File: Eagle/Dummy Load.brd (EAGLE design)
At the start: 100 x 50 mm, 60 parts, among them IC1 LM324D, IC2 AMS1117, IC3 LM35CZ, J2 DCJ0202, X1 MINI-USB-32005-301

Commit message: Update Proteus Files & Latest BRD Version
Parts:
- moved GOLD_ORB_SM2 2.00 mm to (50.1, 24.4)
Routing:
- net VCC: track 280.7 -> 344.2 mm
- net VG: track 76.8 -> 81.7 mm
- net N$15: track 16.8 -> 17.7 mm
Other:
- board text added: "FAN"

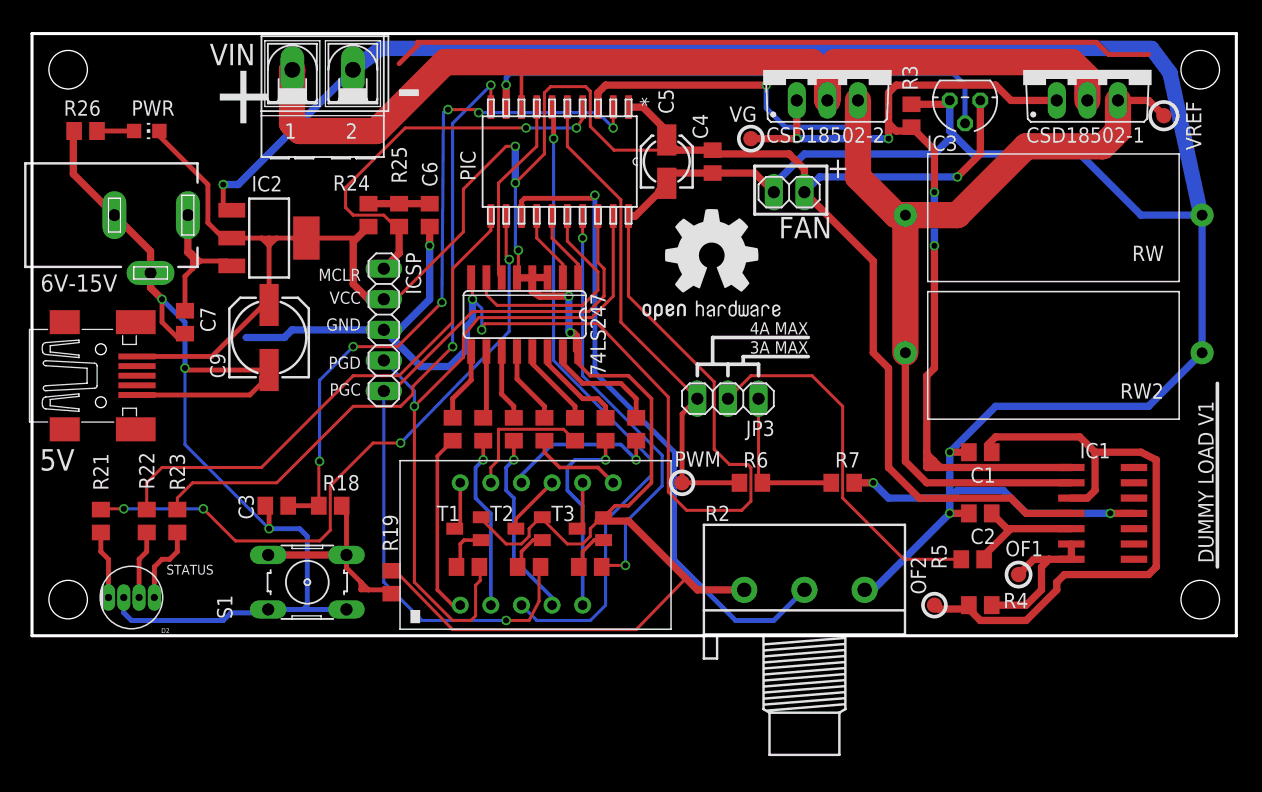
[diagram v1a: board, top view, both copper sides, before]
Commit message: Update all files to V1.1
Implement Gate Series Resistor on MOSFET, to prevent the oscillators in
the output. Also implement new OPAMP LMC662, and new desing of PCB
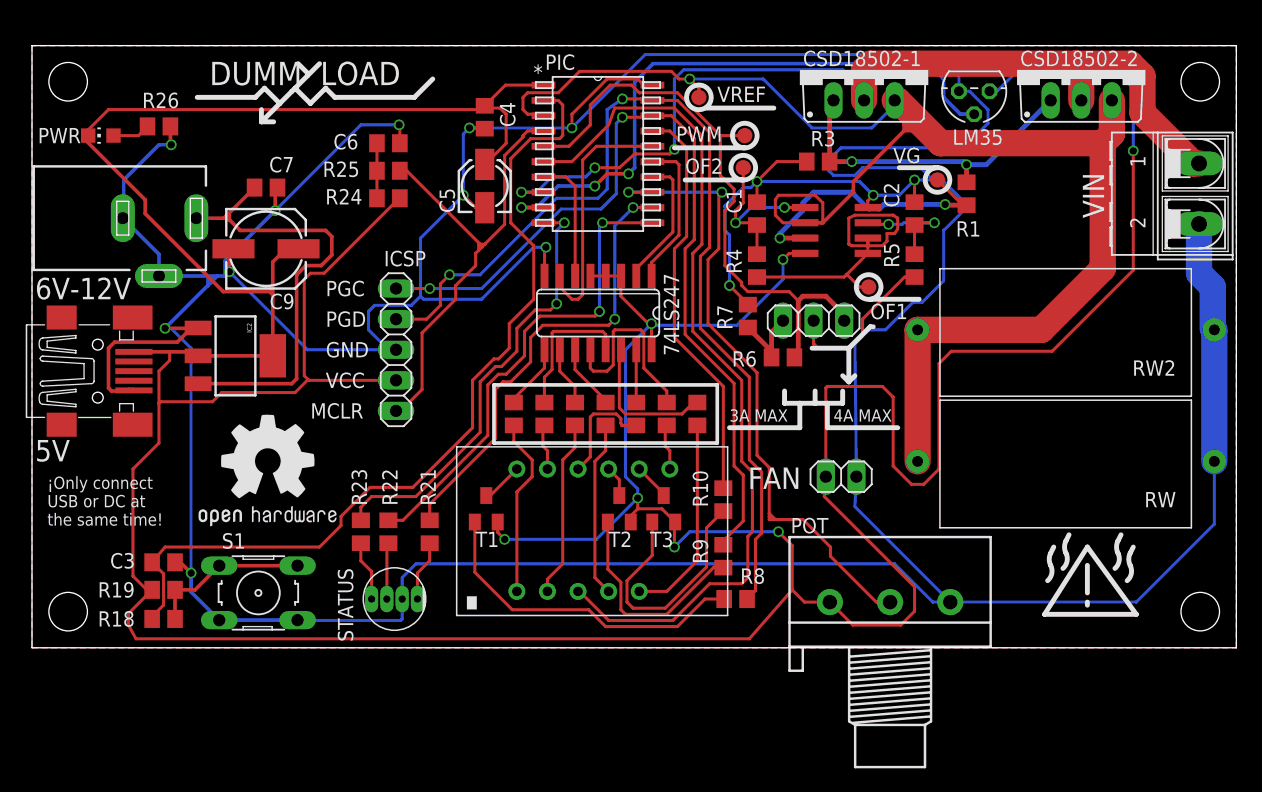
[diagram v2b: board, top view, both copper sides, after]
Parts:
- removed IC1: LM324D, linear:SO14
- removed IC3: LM35CZ, lm35:TO92
- removed R2: 20k, pot:3RP/1610N
- added LM35: LM35CZ, lm35:TO92
- added LM662: LMC662, analog-devices:SO8
- added POT: 20k, pot:3RP/1610N
- added R1: 10k, rcl:R0805
- R21: value 330 -> 400
- moved VIN 73.5 mm to (96.9, 36.7), turned to 270 degrees
- moved GOLD_ORB_SM2 40.6 mm to (13.2, 7.37)
- moved OF2 39.6 mm to (59.1, 38.9), turned to 0 degrees
- moved VREF 38.6 mm to (55.4, 44.7)
- moved R4 33.7 mm to (60.2, 30.7), turned to 270 degrees
- moved PWM 29.3 mm to (59.2, 41.5)
- moved R21 27.3 mm to (33.0, 8.64)
- moved C1 27.1 mm to (60.2, 35.1), turned to 90 degrees
- moved OF1 26.9 mm to (69.5, 29.0), turned to 0 degrees
- moved C2 25.5 mm to (73.3, 35.1), turned to 90 degrees
- moved R5 24.9 mm to (73.3, 30.7), turned to 270 degrees
- moved JP2 24.0 mm to (67.2, 13.2), turned to 180 degrees
- moved R8 22.4 mm to (58.4, 3.05)
- moved CSD18502-2 21.1 mm to (87.1, 47.0)
- moved RW 20.5 mm to (96.3, 19.6)
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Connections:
- new net VG1: CSD18502-1.G, CSD18502-2.G, R1.1, R3.2
- net GND: now also LM35.3, LM662.4, POT.3; no longer IC1.11, IC3.3, R2.3
- net N$5: now also LM662.3; no longer IC1.5
- net OF1: now also LM662.1, LM662.2; no longer IC1.6, IC1.7
- net OF2: now also LM662.5; no longer IC1.3
- net POT: now also POT.2; no longer R2.2
- net TEMP: now also LM35.2; no longer IC3.2
- net VCC: now also LM35.1, LM662.8, POT.1; no longer IC1.4, IC3.1, R2.1
- net VG: now also LM662.7, R1.2; no longer CSD18502-1.G, CSD18502-2.G, IC1.1, R3.2
- net VREF: now also LM662.6; no longer IC1.2
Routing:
- net VG: track 81.7 -> 23.8 mm, vias 4 -> 2
- net VCC: track 344.2 -> 399.9 mm, vias 6 -> 7
- net OF2: track 52.2 -> 15.4 mm, vias 0 -> 2
- net VG1: track 0.00 -> 27.3 mm, vias 0 -> 2
- net VREF: track 101.6 -> 127.7 mm
- net N$3: track 3.90 -> 27.7 mm
- net VJACK: track 14.6 -> 38.3 mm
- net D1: track 58.3 -> 81.2 mm, vias 1 -> 2
- net DP: track 54.4 -> 72.1 mm, vias 1 -> 0
- net BL: track 54.3 -> 36.6 mm
- net N$4: track 3.53 -> 21.0 mm
- net PWI: track 30.9 -> 13.7 mm
- net R: track 54.2 -> 38.1 mm, vias 4 -> 2
- net N$7: track 3.53 -> 18.1 mm
- net SW1: track 58.3 -> 72.7 mm, vias 6 -> 0
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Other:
- board text added: "6V-12V"
- board text added: "DUMM LOAD"
- board text added: "https://github.com/CarlosRodriguezF/Dummy-Load"
- board text added: "¡Only connect USB or DC at the same time!"
- board text removed: "+"
- board text removed: "-"
- board text removed: "6V-15V"
- board text removed: "DUMMY LOAD V1"
